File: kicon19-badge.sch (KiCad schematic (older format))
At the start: 60 parts, among them J1 LogicProbes, J2 Ports, J6 Conn_ARM_JTAG_SWD_20, J7 USB_B_Micro, SW1 BTN1, SW2 BTN2, SW3 BTN3, SW4 BTN4, SW5 Reset, SW6 Erase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

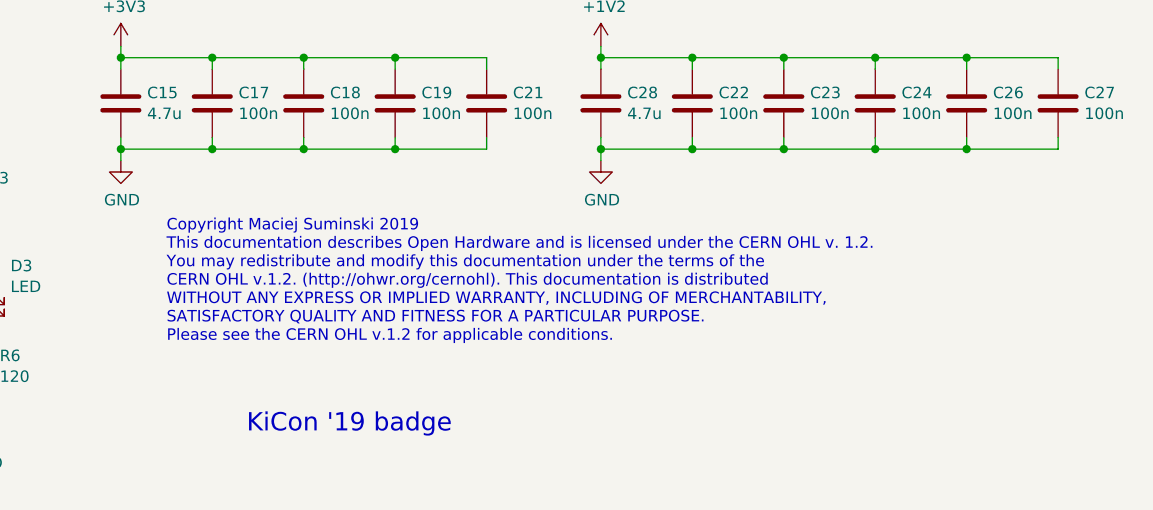
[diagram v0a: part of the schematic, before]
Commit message: Relicensed the design to CERN-OHL-S v2 or later
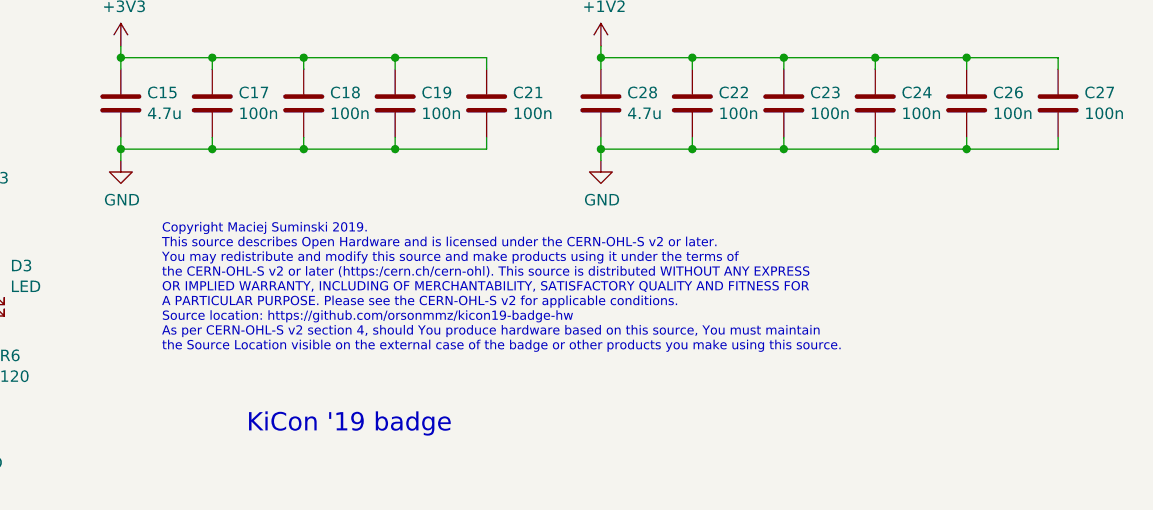
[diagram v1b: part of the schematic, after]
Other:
- note added: "Copyright Maciej Suminski 2019.\nThis source describes Open Hardware and is licensed under the CERN-OHL-S v2 or later.\nYou may redistribute and modify this source and make products using it under the terms of\nthe CERN-OHL-S v2 or later (https:/cern.ch/cern-ohl). This source is distributed WITHOUT ANY EXPRESS\nOR IMPLIED WARRANTY, INCLUDING OF MERCHANTABILITY, SATISFACTORY QUALITY AND FITNESS FO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"
- note removed: "Copyright Maciej Suminski 2019\nThis documentation describes Open Hardware and is licensed under the CERN OHL v. 1.2.\nYou may redistribute and modify this documentation under the terms of the\nCERN OHL v.1.2. (http://ohwr.org/cernohl). This documentation is distributed\nWITHOUT ANY EXPRESS OR IMPLIED WARRANTY, INCLUDING OF MERCHANTABILITY,\nSATISFACTORY QUALITY AND FITNESS FOR A PARTICULAR PURPO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"
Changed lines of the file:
@@
 	-1   0    0    1
 $EndComp
-Text Notes 7000 7100 0    50   ~ 0
-Copyright Maciej Suminski 2019\nThis documentation describes Open Hardware and is licensed under the CERN OHL v. 1.2.\nYou may redistribute and modify this documentation under the terms of the\nCERN OHL v.1.2. (http://ohwr.org/cernohl). This documentation is distributed\nWITHOUT ANY EXPRESS OR IMPLIED WARRANTY, INCLUDING OF MERCHANTABILITY,\nSATISFACTORY QUALITY AND FITNESS FOR A PARTICULAR PURPOSE.\nPlease see the CERN OHL v.1.2 for applicable conditions.
+Text Notes 6980 7140 0    40   ~ 0
+Copyright Maciej Suminski 2019.\nThis source describes Open Hardware and is licensed under the CERN-OHL-S v2 or later.\nYou may redistribute and modify this source and make products using it under the terms of\nthe CERN-OHL-S v2 or later (https:/cern.ch/cern-ohl). This source is distributed WITHOUT ANY EXPRESS\nOR IMPLIED WARRANTY, INCLUDING OF MERCHANTABILITY, SATISFACTORY QUALITY AND FITNESS FOR\nA PARTICULAR PURPOSE. Please see the CERN-OHL-S v2 for applicable conditions.\nSource location: https://github.com/orsonmmz/kicon19-badge-hw\nAs per CERN-OHL-S v2 section 4, should You produce hardware based on this source, You must maintain\nthe Source Location visible on the external case of the badge or other products you make using this source.
 Wire Bus Line
 	1500 4000 1500 4700
